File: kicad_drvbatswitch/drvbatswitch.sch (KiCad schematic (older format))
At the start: 31 parts, among them P1 V_IN+, P2 V_IN-, P3 uC_IN, P4 V_OUT+, P5 V_OUT-, Q1 IRLML6344, Q2 IPD90P03

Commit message: In Kicad geänderte Symbole "gerettet".
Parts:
- D1: symbol LED -> LED-RESCUE-drvbatswitch
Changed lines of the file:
@@
 EESchema Schematic File Version 2
+LIBS:drvbatswitch-rescue
 LIBS:power
 LIBS:device
@@
 LIBS:valves
 LIBS:Custom
+LIBS:drvbatswitch-cache
 EELAYER 25 0
 EELAYER END
@@
 $EndComp
 $Comp
-L LED D1
+L LED-RESCUE-drvbatswitch D1
 U 1 1 57C81BD8
 P 5600 3550

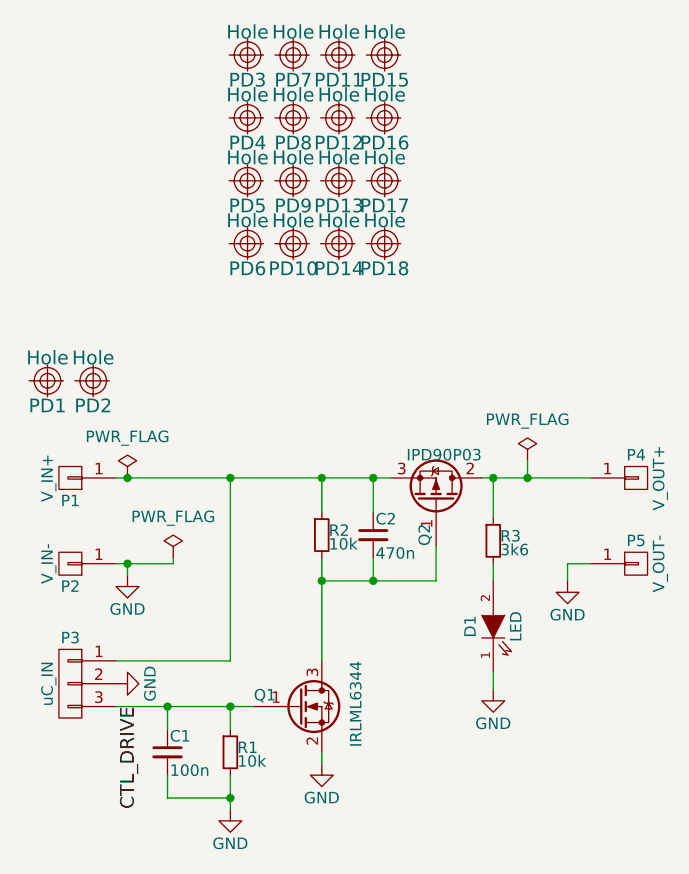
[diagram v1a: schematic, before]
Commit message: Spezifikation D1 nachgetragen.
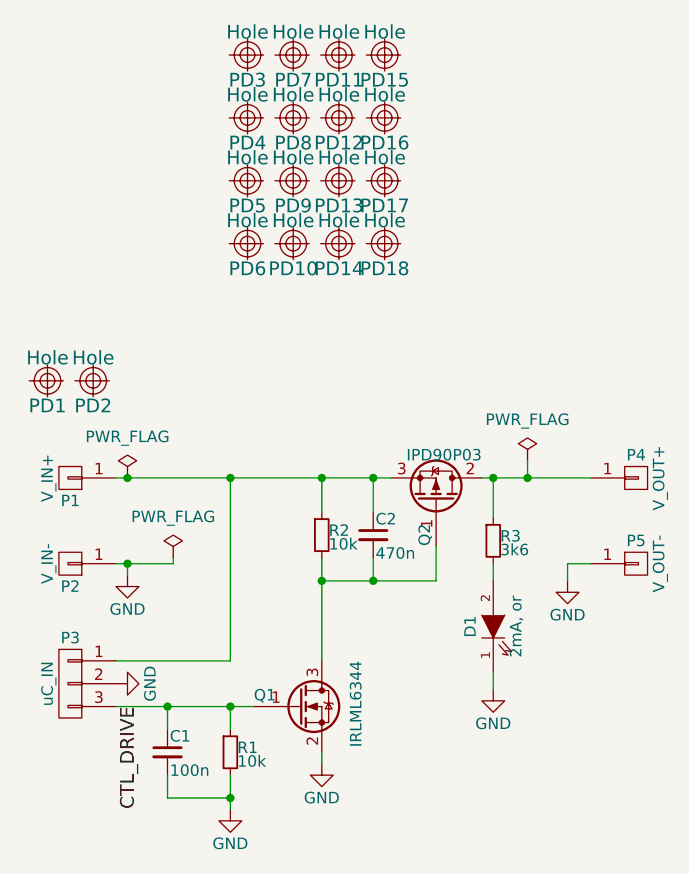
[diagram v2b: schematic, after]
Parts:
- D1: value LED -> 2mA, or
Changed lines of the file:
@@
 P 5600 3550
 F 0 "D1" H 5600 3650 50  0000 C CNN
-F 1 "LED" H 5600 3450 50  0000 C CNN
+F 1 "2mA, or" H 5600 3450 50  0000 C CNN
 F 2 "Custom:LED_0603_HandSoldering" H 5600 3550 50  0001 C CNN
 F 3 "" H 5600 3550 50  0000 C CNN
